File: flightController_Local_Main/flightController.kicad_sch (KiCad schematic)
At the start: 21 parts, among them J1 U.FL-R-SMT10, J2 Conn_ARM_SWD, U2 TESEO-LIV3F, U3 DPS368XTSA1, U4 STM32H723VETx, U6 TPS562201DDCR

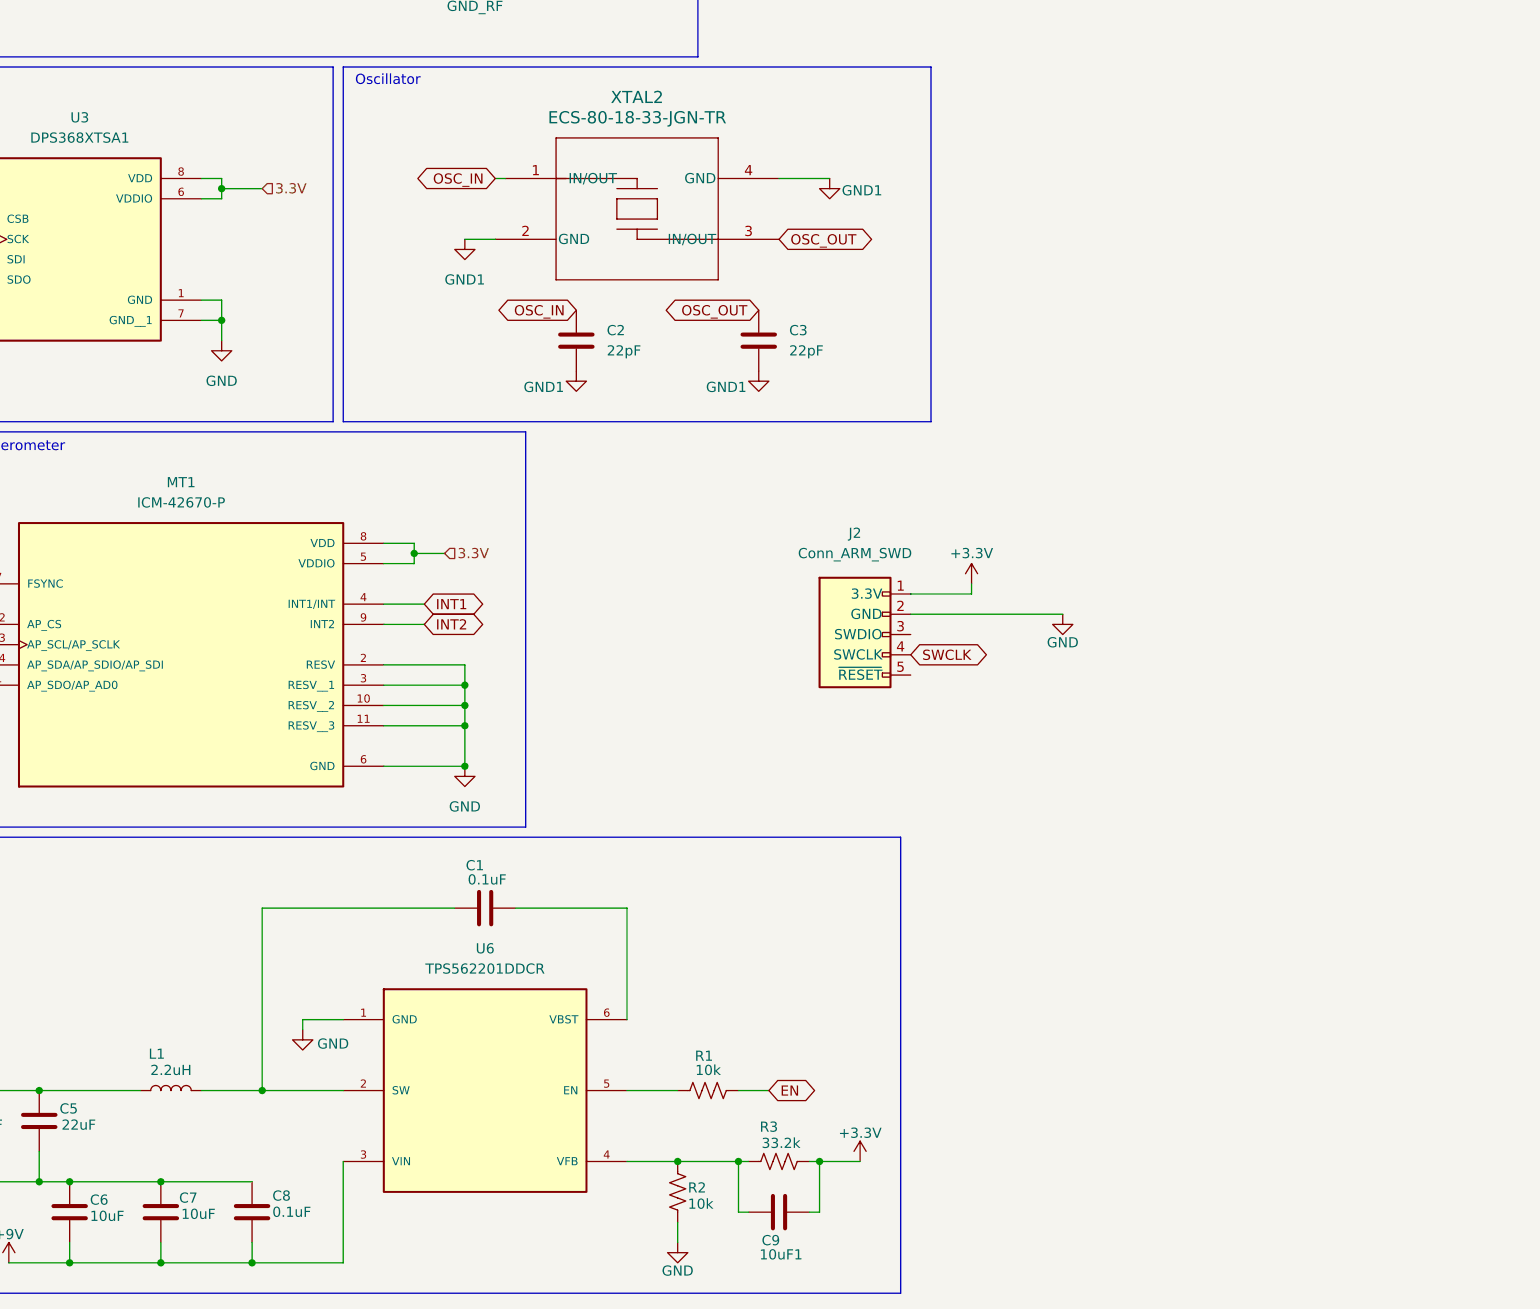
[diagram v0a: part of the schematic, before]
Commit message: adding footprints and models for buck
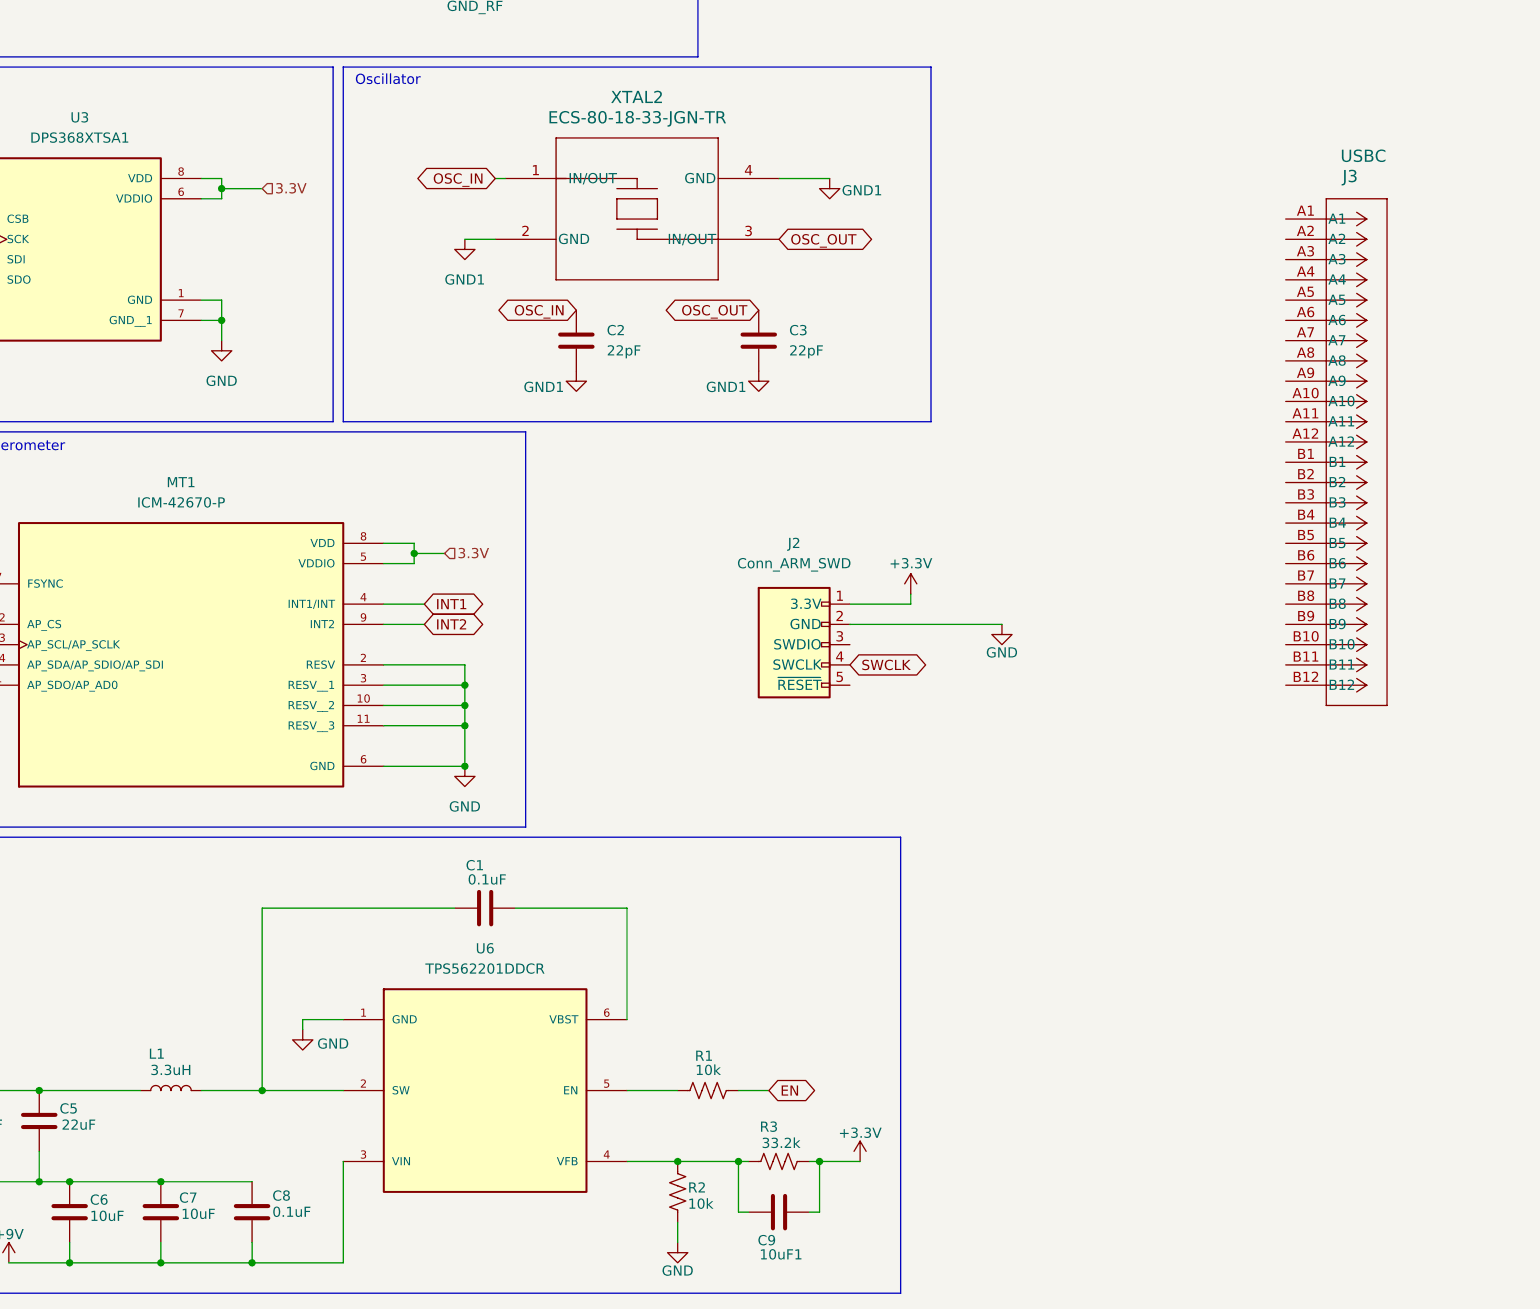
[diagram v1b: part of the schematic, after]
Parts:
- added J3: USBC, Connector_USB:USB_C_Receptacle_Molex_105450-0101, symbol usbc:1054500101
- 10uF1, C6, C7: footprint (none) -> Library:10uF_cap
- C1, C8: footprint (none) -> Library:01uF_CAP
- C4, C5: footprint (none) -> Library:22Uf_CAP
- L1: value 2.2uH -> 3.3uH; footprint (none) -> Library:3_3_Inductor
- R1, R2: footprint (none) -> Library:10kResistor
- R3: footprint (none) -> Library:33.2Resistor
- U6: footprint TPS562201DDCR:SOT95P280X110-6N -> Library:3.3Buck
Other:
- moved on the sheet: J2

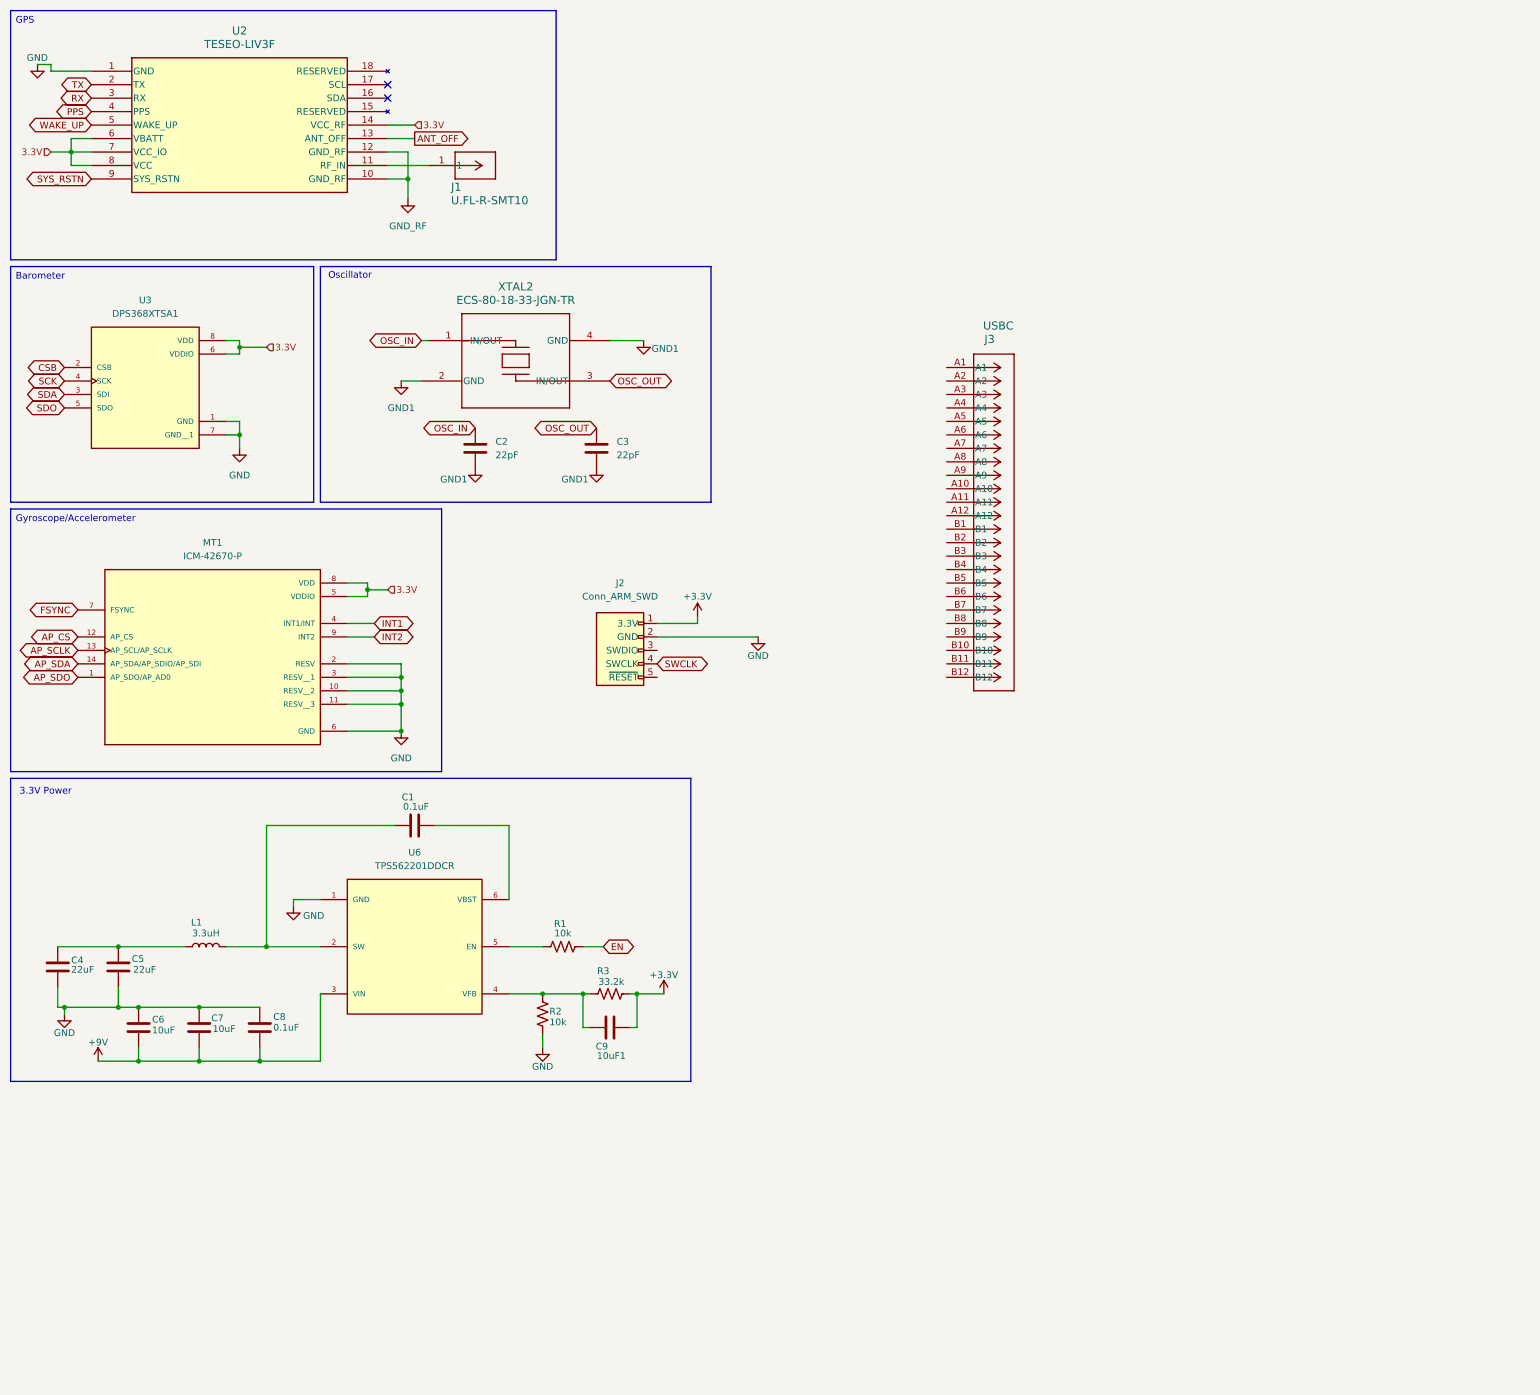
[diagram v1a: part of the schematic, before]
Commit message: Adding caps to IMU and Barometer
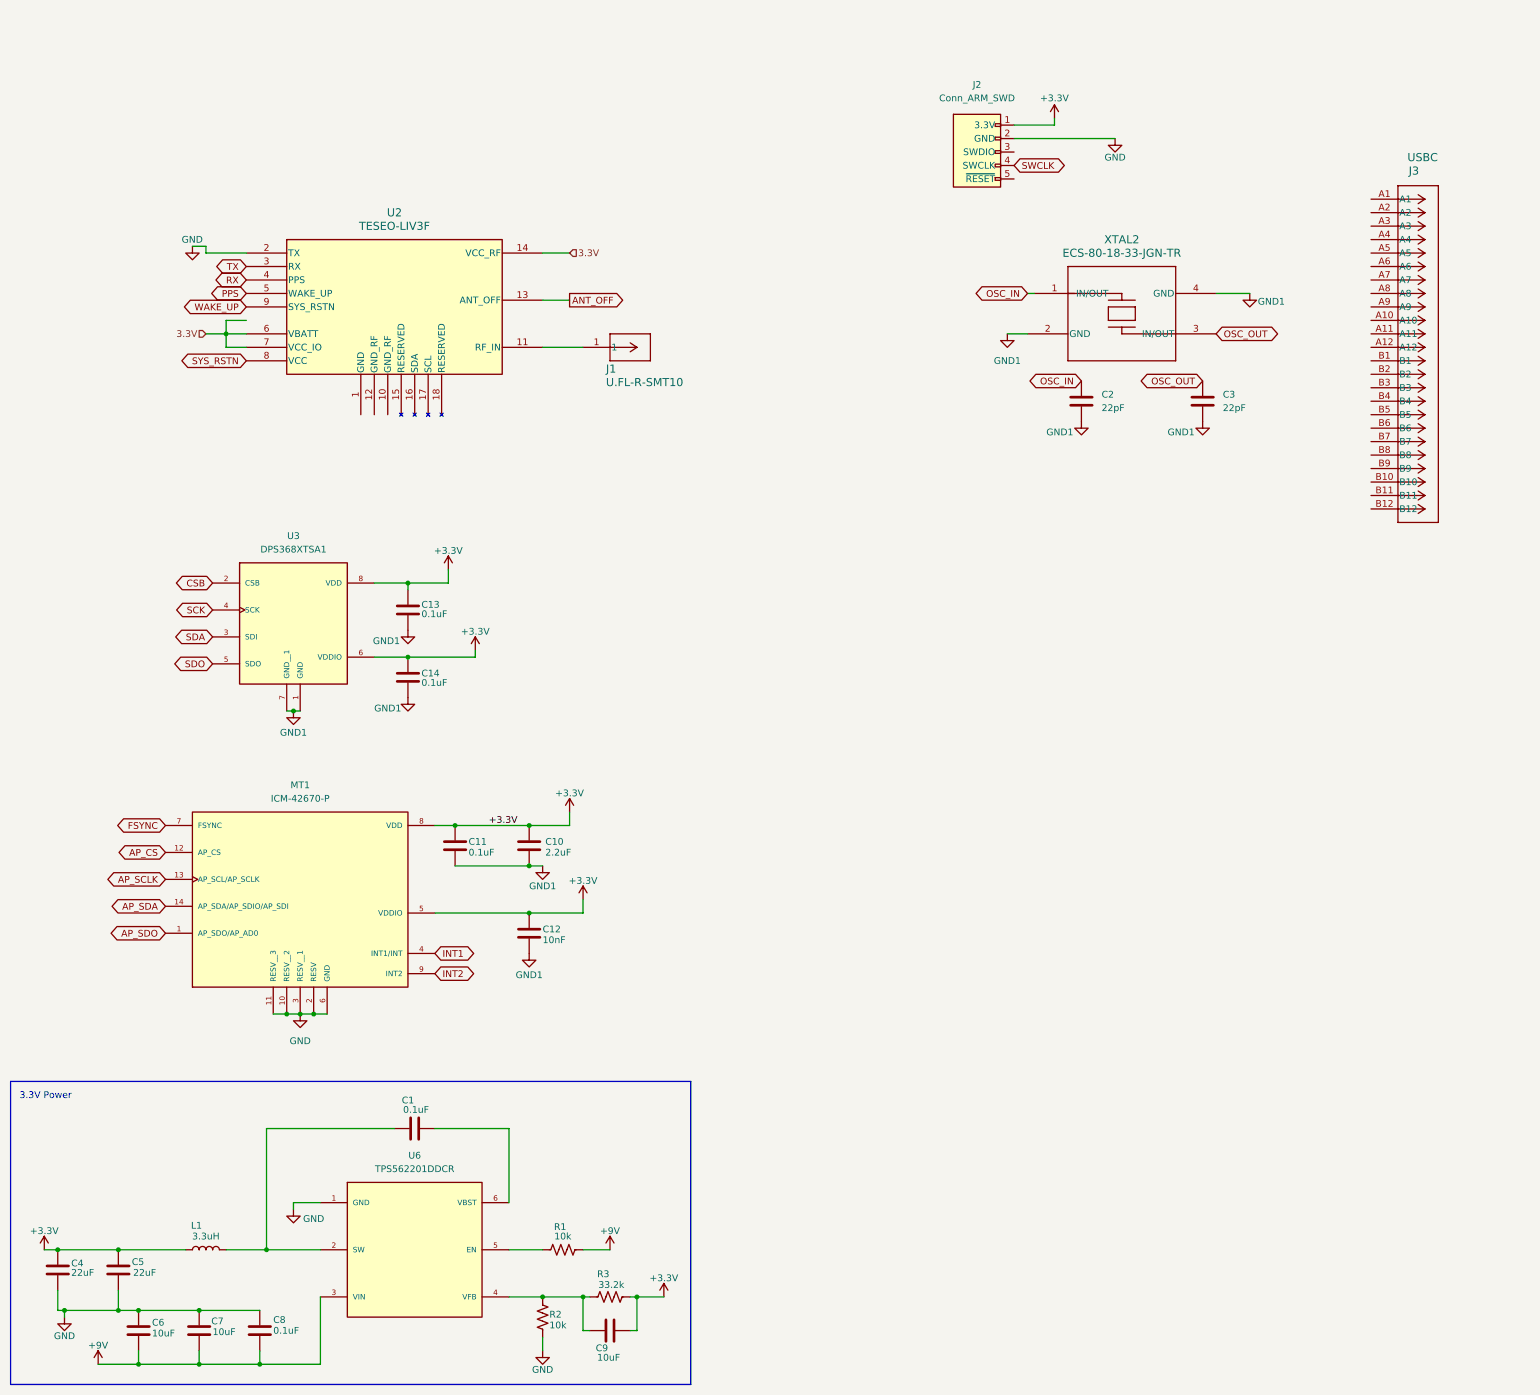
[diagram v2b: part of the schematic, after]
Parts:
- added C10: 2.2uF, Library:2.2uF_CAP_0603, symbol Device:C
- added C11, C13, C14: 0.1uF, Library:01uF_Cap_0603, symbol Device:C
- added C12: 10nF, Library:01uF_Cap_0603, symbol Device:C
- C9: renamed from 10uF1; value C9 -> 10uF
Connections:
- net EN is gone; now on net +9V: R1.2
- net +3.3V: now also C4.1, C5.1, L1.1, MT1.5 (VDDIO), MT1.8 (VDD), U3.6 (VDDIO), U3.8 (VDD), C10.1, C11.1, C12.1, C13.1, C14.1
- net 3.3V: no longer MT1.5 (VDDIO), MT1.8 (VDD), U2.8 (VCC), U3.6 (VDDIO), U3.8 (VDD)
- net GND: now also U2.2 (TX); no longer U2.1 (GND), U3.1 (GND), U3.7 (GND__1)
- net GND1: now also U3.1 (GND), U3.7 (GND__1), C10.2, C11.2, C12.2, C13.2, C14.2
- net PPS: now also U2.5 (WAKE_UP); no longer U2.4 (PPS)
- net RX: now also U2.4 (PPS); no longer U2.3 (RX)
- net SYS_RSTN: now also U2.8 (VCC); no longer U2.9 (SYS_RSTN)
- net TX: now also U2.3 (RX); no longer U2.2 (TX)
- net WAKE_UP: now also U2.9 (SYS_RSTN); no longer U2.5 (WAKE_UP)
- net GND_RF: no longer names the net of U2.10 (GND_RF)
- net GND_RF: no longer U2.12 (GND_RF)
- no-connect marks 2 -> 0
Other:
- note removed: "Oscillator"
- moved on the sheet: C1, C2, C3, C4, C5, C6, C7, C8, C9, J1, J2, J3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

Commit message: Making changes to GPS
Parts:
- added C15: 100nF, symbol Device:C
- added R4: 10k, symbol Device:R_US
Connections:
- net +3.3V: now also U2.6 (VBATT), U2.7 (VCC_IO), U2.8 (VCC), C15.1
- net ANT_OFF: now also R4.1
- net GND: no longer U2.2 (TX)
- net GND1: now also U2.1 (GND), U2.10 (GND_RF), U2.12 (GND_RF), C15.2, R4.2
- net PPS: now also U2.4 (PPS); no longer U2.5 (WAKE_UP)
- net RX: now also U2.3 (RX); no longer U2.4 (PPS)
- net SYS_RSTN: now also U2.9 (SYS_RSTN); no longer U2.8 (VCC)
- net TX: now also U2.2 (TX); no longer U2.3 (RX)
- net WAKE_UP: now also U2.5 (WAKE_UP); no longer U2.9 (SYS_RSTN)
- net at J1.1: no longer U2.11 (RF_IN)
- removed net 3.3V: U2.14 (VCC_RF), U2.6 (VBATT), U2.7 (VCC_IO)
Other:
- moved on the sheet: J1, U2
